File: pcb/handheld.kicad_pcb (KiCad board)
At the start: 2 copper layers, 170.4 x 140.6 mm, 17 parts, among them J1 Conn_01x15_Pin, J2 Conn_01x15_Pin, J3 Conn_02x13_Odd_Even, J4 SD MODULE, SW1 SW_Push, SW10 SW_Push, SW11 SW_Push, SW12 SW_Push, SW2 SW_Push, SW3 SW_Push, SW4 SW_Push, SW5 SW_Push, SW6 SW_Push, SW7 SW_Push, SW8 SW_Push, SW9 SW_Push, U1 MCP23017x-x-SP

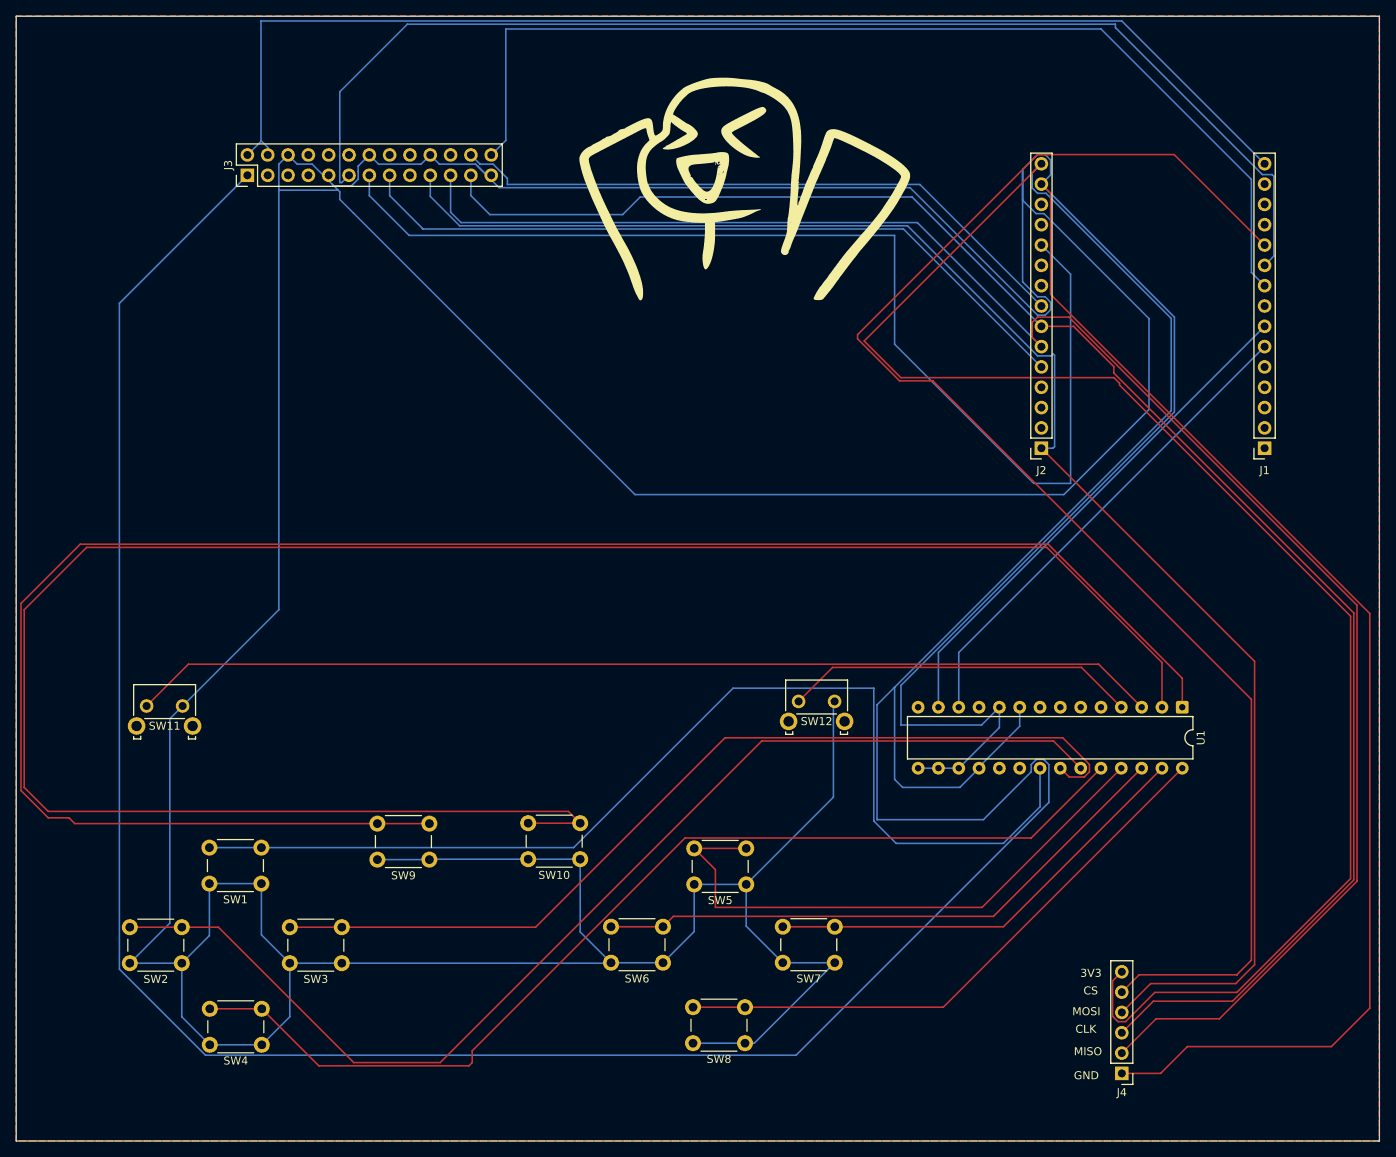
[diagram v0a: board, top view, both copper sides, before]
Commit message: udpated imgs, correct distance between headers
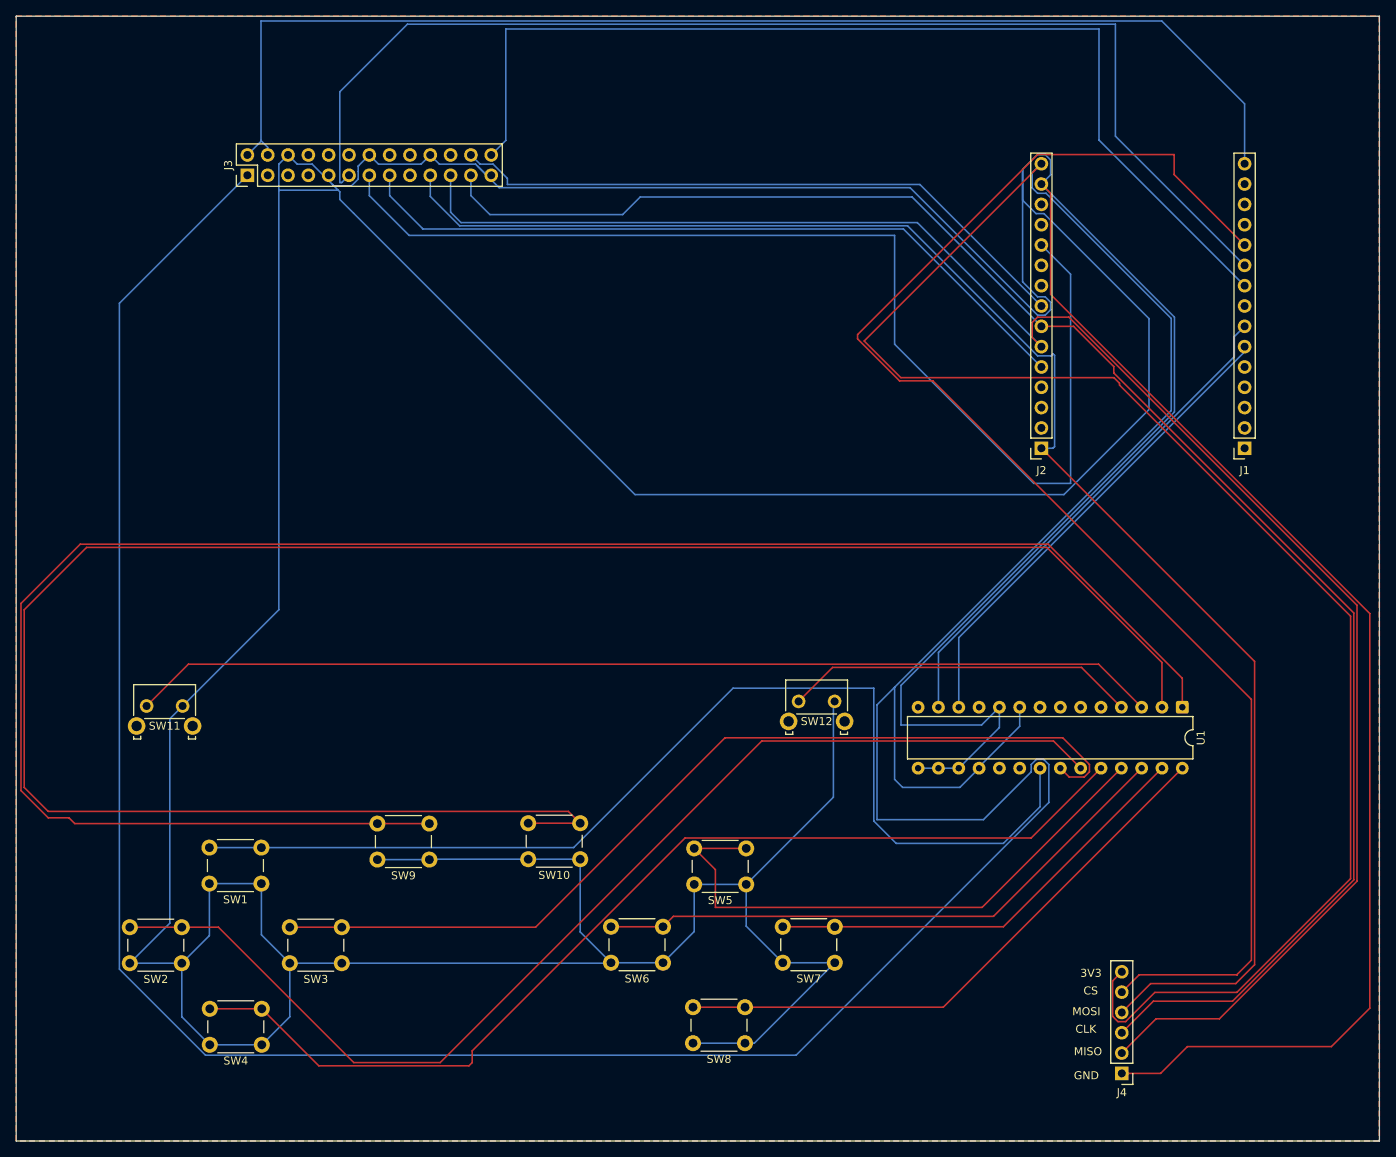
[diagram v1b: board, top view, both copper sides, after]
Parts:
- moved J1 2.50 mm to (165.0, 65.7)
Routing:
- net /GPIO 27: track 152.9 -> 150.2 mm
- net +5V: track 152.4 -> 154.3 mm
- net /GPIO 26: track 131.5 -> 130.3 mm
- net /GPIO 14: track 183.8 -> 182.8 mm
- net /GPIO 33: track 64.5 -> 63.5 mm
- net /GPIO 32: track 60.9 -> 59.9 mm
